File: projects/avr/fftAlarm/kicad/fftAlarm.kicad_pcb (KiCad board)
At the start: 2 copper layers, 76.2 x 35.6 mm, 28 parts, among them P1 CONN_1, P2 CONN_1, P3 CONN_1, P5 CONN_6, Q1 NPN, Q2 NPN, U1 ATTINY85-20PU, U2 7805

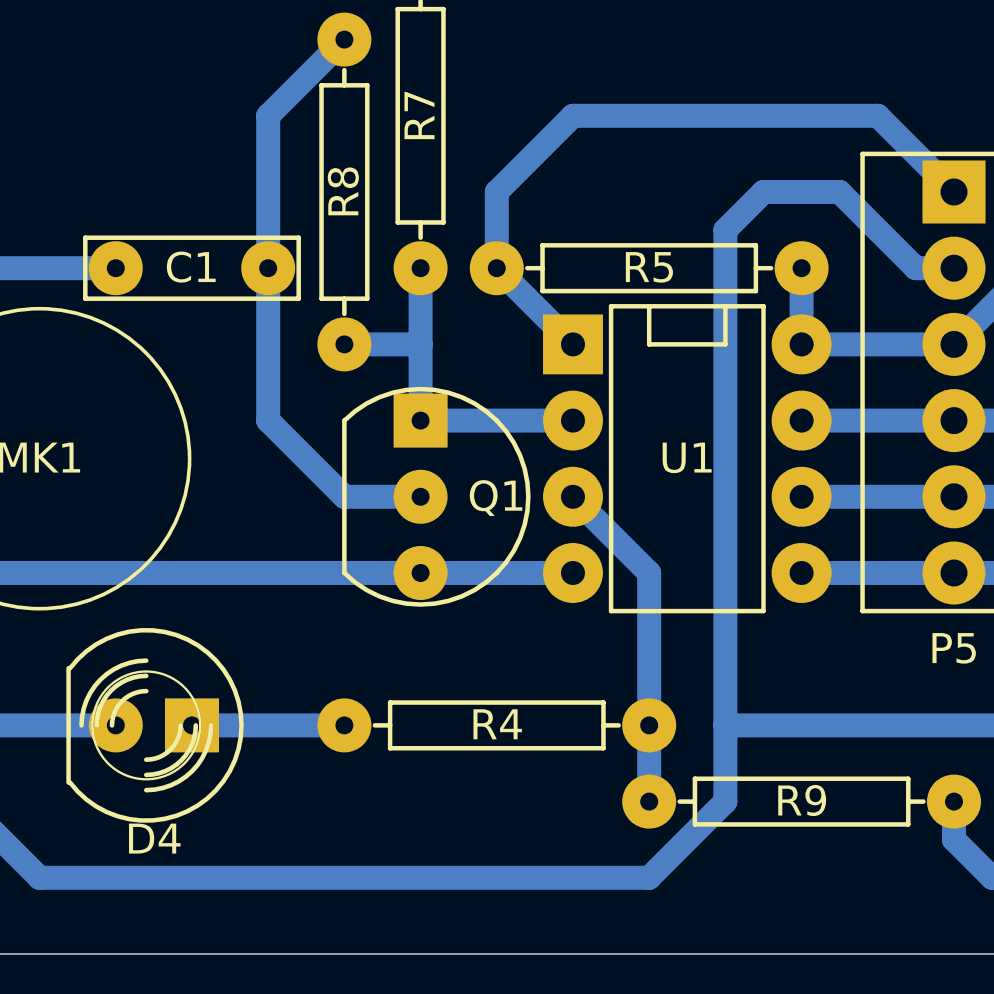
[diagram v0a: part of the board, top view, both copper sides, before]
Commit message: fftAlarm: forgotten capacitor
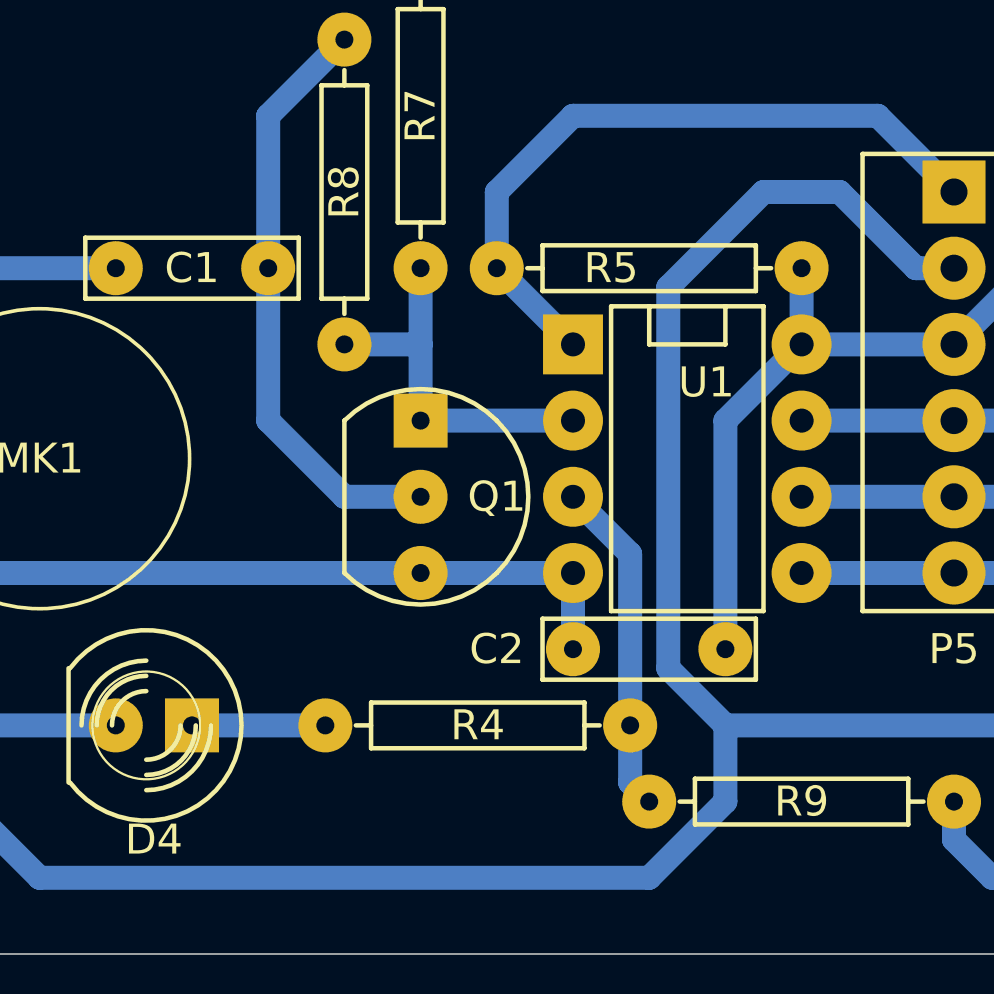
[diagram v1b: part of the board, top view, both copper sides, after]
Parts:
- added C2: C, kicad:C2, F.Cu at (127.0, 63.5)
- moved R4 0.64 mm to (121.3, 66.0)
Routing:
- net Net-(C2-Pad1): track 70.7 -> 81.9 mm
- net Net-(C2-Pad2): track 139.6 -> 143.7 mm
- net Net-(D4-Pad1): track 5.08 -> 4.44 mm

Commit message: update kicad files
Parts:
- C1, C2: footprint kicad:C2 -> common:C2
- D1, D2, D3, D4: footprint kicad:LED-5MM -> common:LED-5MM
- JP1: footprint kicad:PIN_ARRAY_2X1 -> common:PIN_ARRAY_2X1
- MK1: footprint kicad:ELECTRET -> common:ELECTRET
- P1, P2, P3: footprint kicad:PIN_ARRAY_1X1 -> common:PIN_ARRAY_1X1
- P5: footprint kicad:PIN_ARRAY_6X1 -> common:PIN_ARRAY_6X1
- Q1, Q2: footprint kicad:NPN -> common:NPN
- R1, R2, R3, R4, R5, R6, R7, R8, R9: footprint kicad:R4 -> common:R4
- REF** (x4): footprint kicad:ENTRETOISE -> common:ENTRETOISE
- U1: footprint kicad:DIP-8__300 -> common:DIP-8__300
- U2: footprint kicad:TO220_VERT -> common:TO220_VERT
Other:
- net class Default removed
